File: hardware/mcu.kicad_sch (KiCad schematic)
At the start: 17 parts, among them J301 TagConnect, U301 STM32G431, U302 SN65HVD230, Y301 12MHz

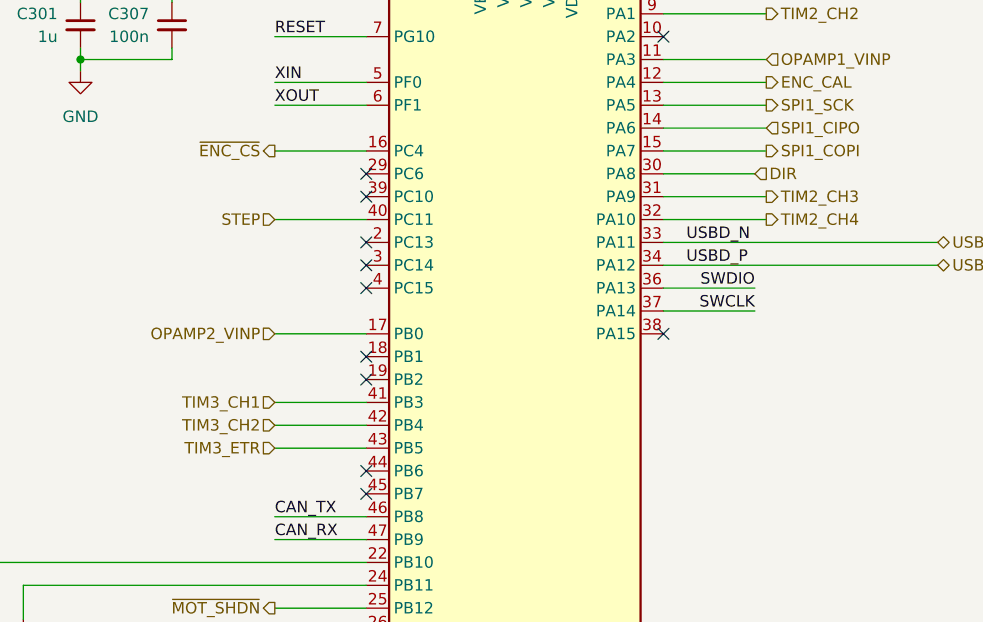
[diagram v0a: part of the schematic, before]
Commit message: start working on current sense
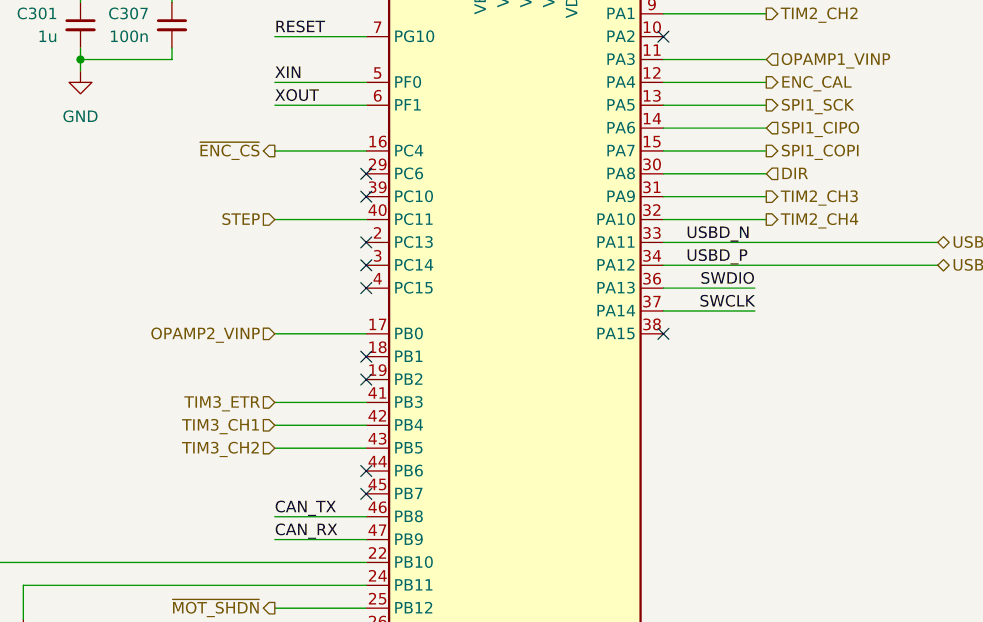
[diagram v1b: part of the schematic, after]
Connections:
- net TIM3_CH1: now also U301.42 (PB4); no longer U301.41 (PB3)
- net TIM3_CH2: now also U301.43 (PB5); no longer U301.42 (PB4)
- net TIM3_ETR: now also U301.41 (PB3); no longer U301.43 (PB5)
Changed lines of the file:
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@@
     (stroke (width 0) (type default))
   )
-  (wire (pts (xy 127 90.17) (xy 116.84 90.17))
+  (wire (pts (xy 128.27 90.17) (xy 116.84 90.17))
     (stroke (width 0) (type default))
   )
@@
     (effects (font (size 1.27 1.27)) (justify left))
   )
-  (hierarchical_label "TIM3_CH1" (shape input) (at 73.66 115.57 180) (fields_autoplaced)
+  (hierarchical_label "TIM3_CH1" (shape input) (at 73.66 118.11 180) (fields_autoplaced)
     (effects (font (size 1.27 1.27)) (justify right))
   )
@@
     (effects (font (size 1.27 1.27)) (justify right))
   )
-  (hierarchical_label "TIM3_ETR" (shape input) (at 73.66 120.65 180) (fields_autoplaced)
-    (effects (font (size 1.27 1.27)) (justify right))
-  )
-  (hierarchical_label "TIM3_CH2" (shape input) (at 73.66 118.11 180) (fields_autoplaced)
+  (hierarchical_label "TIM3_ETR" (shape input) (at 73.66 115.57 180) (fields_autoplaced)
+    (effects (font (size 1.27 1.27)) (justify right))
+  )
+  (hierarchical_label "TIM3_CH2" (shape input) (at 73.66 120.65 180) (fields_autoplaced)
     (effects (font (size 1.27 1.27)) (justify right))
   )
@@
     (effects (font (size 1.27 1.27)) (justify right))
   )
-  (hierarchical_label "DIR" (shape input) (at 127 90.17 0) (fields_autoplaced)
-    (effects (font (size 1.27 1.27)) (justify left))
-  )
+  (hierarchical_label "DIR" (shape input) (at 128.27 90.17 0) (fields_autoplaced)
+    (effects (font (size 1.27 1.27)) (justify left))
+  )

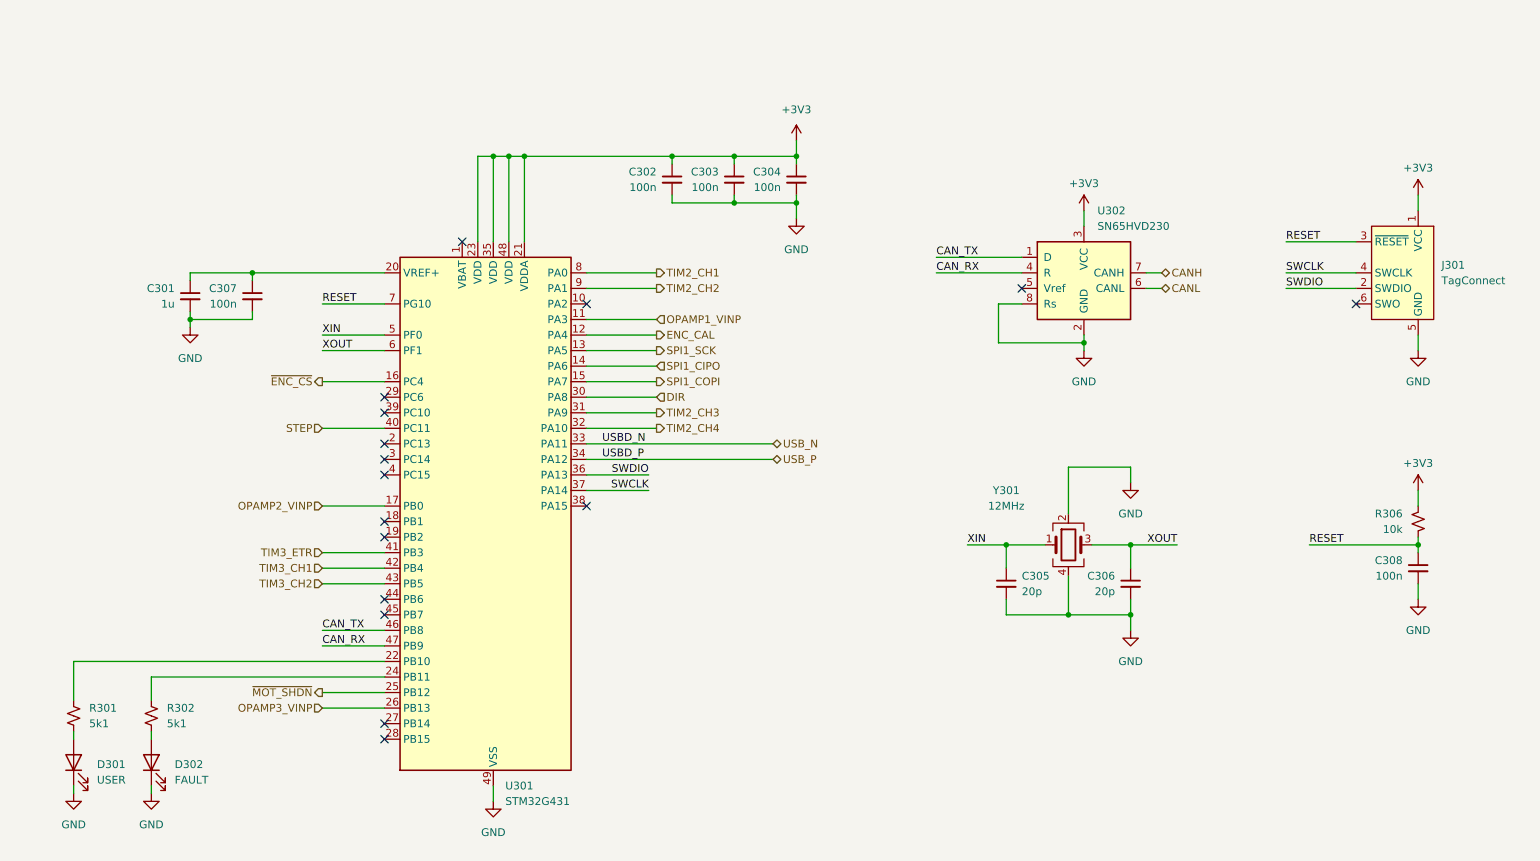
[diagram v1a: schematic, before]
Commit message: redraw USB C connector with proper mounting holes
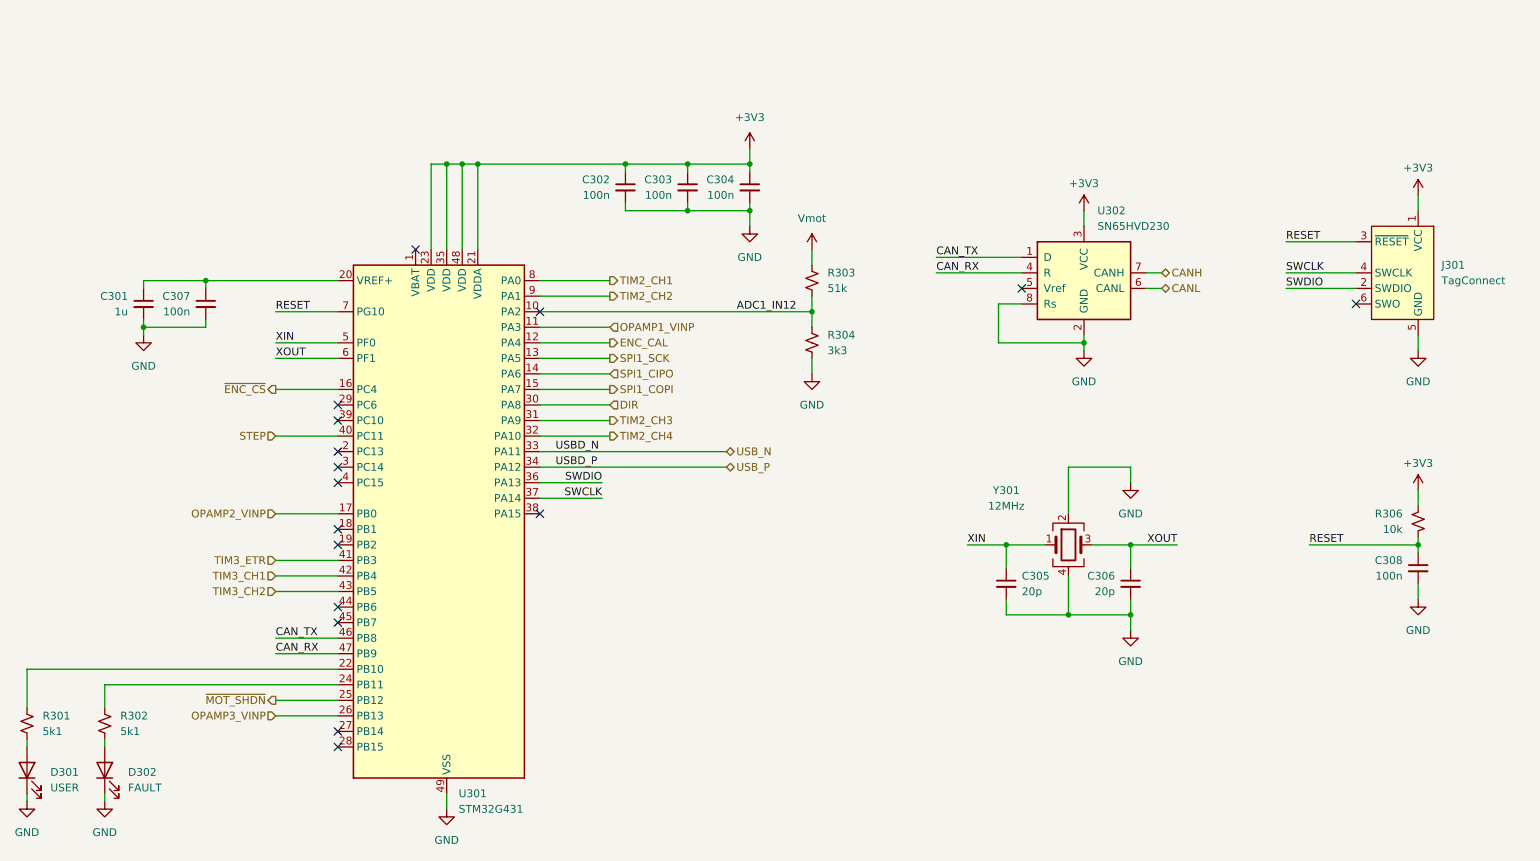
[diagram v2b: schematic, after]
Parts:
- added R303: 51k, Resistor_SMD:R_0402_1005Metric, symbol Device:R_Small_US
- added R304: 3k3, Resistor_SMD:R_0402_1005Metric, symbol Device:R_Small_US
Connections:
- net GND: now also R304.2
- net ADC1_IN12: now reaches U301.10 (PA2)
- net ADC1_IN12: now also R303.2, R304.1
- new net Vmot: R303.1
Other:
- moved on the sheet: C301, C302, C303, C304, C307, D301, D302, R301, R302, U301

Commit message: work on current sense
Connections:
- net DIR: now also U301.39 (PC10)
- no-connect marks 16 -> 15
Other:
- note added: "really acting as UART3"
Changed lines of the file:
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@@
   (no_connect (at 242.57 74.93))
   (no_connect (at 76.2 147.32))
-  (no_connect (at 76.2 93.98))
   (no_connect (at 109.22 109.22))
   (no_connect (at 109.22 76.2))
@@
     (stroke (width 0) (type default))
   )
+  (wire (pts (xy 66.04 93.98) (xy 76.2 93.98))
+    (stroke (width 0) (type default))
+  )
   (wire (pts (xy 153.67 73.66) (xy 153.67 76.2))
     (stroke (width 0) (type default))
@@
   (wire (pts (xy 198.12 81.28) (xy 198.12 82.55))
     (stroke (width 0) (type default))
+  )
+  (text "really acting as UART3" (at 38.1 93.98 0)
+    (effects (font (size 1.27 1.27)) (justify left bottom))
   )
   (label "ADC1_IN12" (at 151.13 76.2 180) (fields_autoplaced)
@@
     (effects (font (size 1.27 1.27)) (justify left))
   )
+  (hierarchical_label "DIR" (shape input) (at 66.04 93.98 180) (fields_autoplaced)
+    (effects (font (size 1.27 1.27)) (justify right))
+  )
   (hierarchical_label "USB_N" (shape bidirectional) (at 139.7 99.06 0) (fields_autoplaced)

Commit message: update pcb layout
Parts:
- added J302: USER CONN., mechanical:PinHeader_1x05_P1.27mm_SMD, symbol Connector_Generic:Conn_01x05
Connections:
- net USER_3: now reaches U301.27 (PB14)
- net USER_3: now also J302.3 (Pin_3)
- net USER_2: now reaches U301.28 (PB15)
- net USER_2: now also J302.4 (Pin_4)
- net USER_1: now reaches U301.29 (PC6)
- net USER_1: now also J302.5 (Pin_5)
- net TIM4_CH1: now reaches U301.44 (PB6)
- net TIM4_CH1: now also J302.1 (Pin_1)
- net TIM4_CH2: now reaches U301.45 (PB7)
- net TIM4_CH2: now also J302.2 (Pin_2)
- no-connect marks 15 -> 10
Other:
- moved on the sheet: C305, C306, C308, J301, R306, U302, Y301
